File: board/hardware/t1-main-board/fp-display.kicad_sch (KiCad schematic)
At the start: 7 parts, among them U5901 TPS22945DCKR

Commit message: Board: capture blk.maskrom
Power + Vol- at a cold power-on pull eMMC D0 low inside the TPS3808G01
boot window (BOM v1 lines 35, 78, 97, 98; sim/maskrom): SENSE 280k/100k,
CT 390 nF, WINDOW_N with its pad, SN74LVC1G57 and SN74LVC1G58 on
vcca1v8_pmu, BAT54 from PWRON_N, DMG1012T through 1 kΩ to EMMC_D0.
Every block in use now has its sheet; the README states the remaining
single-pin nets.

Co-Authored-By: Claude Opus 5.5 <noreply@anthropic.com>
Claude-Session: https://claude.ai/code/session_01Ei262h3TpgY9vyfNLMi5Mn
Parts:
- removed C5901, C5902: 1 µF, Capacitor_SMD:C_0402_1005Metric, symbol Device:C
- removed R5901: 10 kΩ, Resistor_SMD:R_0402_1005Metric, symbol Device:R
- removed R5902: 100 mΩ, Resistor_SMD:R_0603_1608Metric, symbol Device:R
- removed TP5901: FP_VCI_SW, TestPoint:TestPoint_Pad_D1.0mm, symbol Connector:TestPoint
- removed TP5902: FP_VCI, TestPoint:TestPoint_Pad_D1.0mm, symbol Connector:TestPoint
- removed U5901: TPS22945DCKR, Texas_Instruments:Texas_DCK0005A_SC-70-5_1.25x2mm_P0.65mm, symbol Texas_Instruments:TPS22945DCKR
- added C6001, C6002: 1 µF, Capacitor_SMD:C_0402_1005Metric, symbol Device:C
- added R6001: 10 kΩ, Resistor_SMD:R_0402_1005Metric, symbol Device:R
- added R6002: 100 mΩ, Resistor_SMD:R_0603_1608Metric, symbol Device:R
- added TP6001: FP_VCI_SW, TestPoint:TestPoint_Pad_D1.0mm, symbol Connector:TestPoint
- added TP6002: FP_VCI, TestPoint:TestPoint_Pad_D1.0mm, symbol Connector:TestPoint
- added U6001: TPS22945DCKR, Texas_Instruments:Texas_DCK0005A_SC-70-5_1.25x2mm_P0.65mm, symbol Texas_Instruments:TPS22945DCKR
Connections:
- net FP_IO_EN: now also U6001.4 (ON)
- net FP_VCI: now also R6002.2, TP6002.1
- net FP_VCI_SRC: now also C6001.1, U6001.5 (VIN)
- net FP_VCI_SW: now also C6002.1, R6001.1, R6002.1, TP6001.1, U6001.1 (VOUT)
- net GND: now also C6001.2, C6002.2, R6001.2, U6001.2 (GND)
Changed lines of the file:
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@@
 (title_block (title "Faceplate display supply") (date "2026-10-25") (rev "A") (company "The OpenDAP Project") (comment 1 "blk.fp-display") (comment 2 "FP_VCI current-limited switch after RK809 LDO4; DSI lanes pass to the connector"))
 (symbol (lib_id "Texas_Instruments:TPS22945DCKR") (at 48.26 60.96 0) (unit 1) (body_style 1) (exclude_from_sim no) (in_bom yes) (on_board yes) (dnp no)
-  (property "Reference" "U5901" (at 49.53 45.72 0) (effects (font (size 1.27 1.27)) (justify left)))
+  (property "Reference" "U6001" (at 49.53 45.72 0) (effects (font (size 1.27 1.27)) (justify left)))
   (property "Value" "TPS22945DCKR" (at 49.53 43.18 0) (effects (font (size 1.27 1.27)) (justify left)))
   (property "Footprint" "Texas_Instruments:Texas_DCK0005A_SC-70-5_1.25x2mm_P0.65mm" (at 48.26 60.96 0) (effects (font (size 1.27 1.27))) (hide yes))
@@
   (pin "5")
   (pin "2")
-  (instances (project "t1-main-board" (path "/7746052e-d7f9-59ad-ba73-bd2b74439529/996ec8da-1510-50ce-b9cf-a8f3bb19efac" (reference "U5901") (unit 1))))
+  (instances (project "t1-main-board" (path "/7746052e-d7f9-59ad-ba73-bd2b74439529/996ec8da-1510-50ce-b9cf-a8f3bb19efac" (reference "U6001") (unit 1))))
 )
 (wire (pts (xy 38.1 60.96) (xy 35.56 60.96)) (stroke (width 0) (type default)))
@@
 )
 (symbol (lib_id "Device:C") (at 77.47 55.88 0) (unit 1) (body_style 1) (exclude_from_sim no) (in_bom yes) (on_board yes) (dnp no)
-  (property "Reference" "C5901" (at 80.01 54.61 0) (effects (font (size 1.27 1.27)) (justify left)))
+  (property "Reference" "C6001" (at 80.01 54.61 0) (effects (font (size 1.27 1.27)) (justify left)))
   (property "Value" "1 µF" (at 80.01 57.15 0) (effects (font (size 1.27 1.27)) (justify left)))
   (property "Footprint" "Capacitor_SMD:C_0402_1005Metric" (at 77.47 55.88 0) (effects (font (size 1.27 1.27))) (hide yes))
@@
   (pin "1")
   (pin "2")
-  (instances (project "t1-main-board" (path "/7746052e-d7f9-59ad-ba73-bd2b74439529/996ec8da-1510-50ce-b9cf-a8f3bb19efac" (reference "C5901") (unit 1))))
+  (instances (project "t1-main-board" (path "/7746052e-d7f9-59ad-ba73-bd2b74439529/996ec8da-1510-50ce-b9cf-a8f3bb19efac" (reference "C6001") (unit 1))))
 )
 (wire (pts (xy 77.47 52.07) (xy 77.47 49.53)) (stroke (width 0) (type default)))
@@
 )
 (symbol (lib_id "Device:C") (at 90.17 55.88 0) (unit 1) (body_style 1) (exclude_from_sim no) (in_bom yes) (on_board yes) (dnp no)
-  (property "Reference" "C5902" (at 92.71 54.61 0) (effects (font (size 1.27 1.27)) (justify left)))
+  (property "Reference" "C6002" (at 92.71 54.61 0) (effects (font (size 1.27 1.27)) (justify left)))
   (property "Value" "1 µF" (at 92.71 57.15 0) (effects (font (size 1.27 1.27)) (justify left)))
   (property "Footprint" "Capacitor_SMD:C_0402_1005Metric" (at 90.17 55.88 0) (effects (font (size 1.27 1.27))) (hide yes))
@@
   (pin "1")
   (pin "2")
-  (instances (project "t1-main-board" (path "/7746052e-d7f9-59ad-ba73-bd2b74439529/996ec8da-1510-50ce-b9cf-a8f3bb19efac" (reference "C5902") (unit 1))))
+  (instances (project "t1-main-board" (path "/7746052e-d7f9-59ad-ba73-bd2b74439529/996ec8da-1510-50ce-b9cf-a8f3bb19efac" (reference "C6002") (unit 1))))
 )
 (wire (pts (xy 90.17 52.07) (xy 90.17 49.53)) (stroke (width 0) (type default)))
@@
 )
 (symbol (lib_id "Device:R") (at 102.87 55.88 0) (unit 1) (body_style 1) (exclude_from_sim no) (in_bom yes) (on_board yes) (dnp no)
-  (property "Reference" "R5901" (at 104.14 54.61 0) (effects (font (size 1.27 1.27)) (justify left)))
+  (property "Reference" "R6001" (at 104.14 54.61 0) (effects (font (size 1.27 1.27)) (justify left)))
   (property "Value" "10 kΩ" (at 104.14 57.15 0) (effects (font (size 1.27 1.27)) (justify left)))
   (property "Footprint" "Resistor_SMD:R_0402_1005Metric" (at 102.87 55.88 0) (effects (font (size 1.27 1.27))) (hide yes))
@@
   (pin "1")
   (pin "2")
-  (instances (project "t1-main-board" (path "/7746052e-d7f9-59ad-ba73-bd2b74439529/996ec8da-1510-50ce-b9cf-a8f3bb19efac" (reference "R5901") (unit 1))))
+  (instances (project "t1-main-board" (path "/7746052e-d7f9-59ad-ba73-bd2b74439529/996ec8da-1510-50ce-b9cf-a8f3bb19efac" (reference "R6001") (unit 1))))
 )
 (wire (pts (xy 102.87 52.07) (xy 102.87 49.53)) (stroke (width 0) (type default)))
@@
 (text "FP_VCI: TPS22945 after RK809 LDO4 (BOM v1 line 146)" (exclude_from_sim no) (at 24.13 34.29 0) (effects (font (size 2.54 2.54)) (justify left bottom)))
 (symbol (lib_id "Device:R") (at 181.61 50.8 90) (unit 1) (body_style 1) (exclude_from_sim no) (in_bom yes) (on_board yes) (dnp no)
-  (property "Reference" "R5902" (at 179.07 46.99 90) (effects (font (size 1.27 1.27))))
+  (property "Reference" "R6002" (at 179.07 46.99 90) (effects (font (size 1.27 1.27))))
   (property "Value" "100 mΩ" (at 179.07 53.34 90) (effects (font (size 1.27 1.27))))
   (property "Spec" "0603" (at 179.07 55.88 90) (effects (font (size 1.27 1.27))))
@@
   (pin "1")
   (pin "2")
-  (instances (project "t1-main-board" (path "/7746052e-d7f9-59ad-ba73-bd2b74439529/996ec8da-1510-50ce-b9cf-a8f3bb19efac" (reference "R5902") (unit 1) (variant (name "production") (field (name "Value") (value "0 Ω")) (field (name "MPN") (value "RC0603JR-070RL")) (field (name "Manufacturer") (value "YAGEO"))))))
+  (instances (project "t1-main-board" (path "/7746052e-d7f9-59ad-ba73-bd2b74439529/996ec8da-1510-50ce-b9cf-a8f3bb19efac" (reference "R6002") (unit 1) (variant (name "production") (field (name "Value") (value "0 Ω")) (field (name "MPN") (value "RC0603JR-070RL")) (field (name "Manufacturer") (value "YAGEO"))))))
 )
 (rectangle (start 161.29 38.1) (end 198.12 58.42) (stroke (width 0) (type dash)) (fill (type none)))
@@
 (wire (pts (xy 175.26 50.8) (xy 175.26 48.26)) (stroke (width 0) (type default)))
 (symbol (lib_id "Connector:TestPoint") (at 175.26 48.26 0) (unit 1) (body_style 1) (exclude_from_sim no) (in_bom no) (on_board yes) (dnp no)
-  (property "Reference" "TP5901" (at 173.99 43.18 0) (effects (font (size 1.27 1.27)) (justify right)))
+  (property "Reference" "TP6001" (at 173.99 43.18 0) (effects (font (size 1.27 1.27)) (justify right)))
   (property "Value" "FP_VCI_SW" (at 173.99 45.72 0) (effects (font (size 1.27 1.27)) (justify right)))
   (property "Footprint" "TestPoint:TestPoint_Pad_D1.0mm" (at 175.26 48.26 0) (effects (font (size 1.27 1.27))) (hide yes))
@@
   (property "Block" "blk.fp-display" (at 175.26 48.26 0) (effects (font (size 1.27 1.27))) (hide yes))
   (pin "1")
-  (instances (project "t1-main-board" (path "/7746052e-d7f9-59ad-ba73-bd2b74439529/996ec8da-1510-50ce-b9cf-a8f3bb19efac" (reference "TP5901") (unit 1))))
+  (instances (project "t1-main-board" (path "/7746052e-d7f9-59ad-ba73-bd2b74439529/996ec8da-1510-50ce-b9cf-a8f3bb19efac" (reference "TP6001") (unit 1))))
 )
 (wire (pts (xy 185.42 50.8) (xy 210.82 50.8)) (stroke (width 0) (type default)))
@@
 (wire (pts (xy 187.96 50.8) (xy 187.96 48.26)) (stroke (width 0) (type default)))
 (symbol (lib_id "Connector:TestPoint") (at 187.96 48.26 0) (unit 1) (body_style 1) (exclude_from_sim no) (in_bom no) (on_board yes) (dnp no)
-  (property "Reference" "TP5902" (at 189.23 43.18 0) (effects (font (size 1.27 1.27)) (justify left)))
+  (property "Reference" "TP6002" (at 189.23 43.18 0) (effects (font (size 1.27 1.27)) (justify left)))
   (property "Value" "FP_VCI" (at 189.23 45.72 0) (effects (font (size 1.27 1.27)) (justify left)))
   (property "Footprint" "TestPoint:TestPoint_Pad_D1.0mm" (at 187.96 48.26 0) (effects (font (size 1.27 1.27))) (hide yes))
@@
   (property "Block" "blk.fp-display" (at 187.96 48.26 0) (effects (font (size 1.27 1.27))) (hide yes))
   (pin "1")
-  (instances (project "t1-main-board" (path "/7746052e-d7f9-59ad-ba73-bd2b74439529/996ec8da-1510-50ce-b9cf-a8f3bb19efac" (reference "TP5902") (unit 1))))
+  (instances (project "t1-main-board" (path "/7746052e-d7f9-59ad-ba73-bd2b74439529/996ec8da-1510-50ce-b9cf-a8f3bb19efac" (reference "TP6002") (unit 1))))
 )
 (symbol (lib_id "power:VCC") (at 210.82 50.8 270) (unit 1) (body_style 1) (exclude_from_sim no) (in_bom yes) (on_board yes) (dnp no)

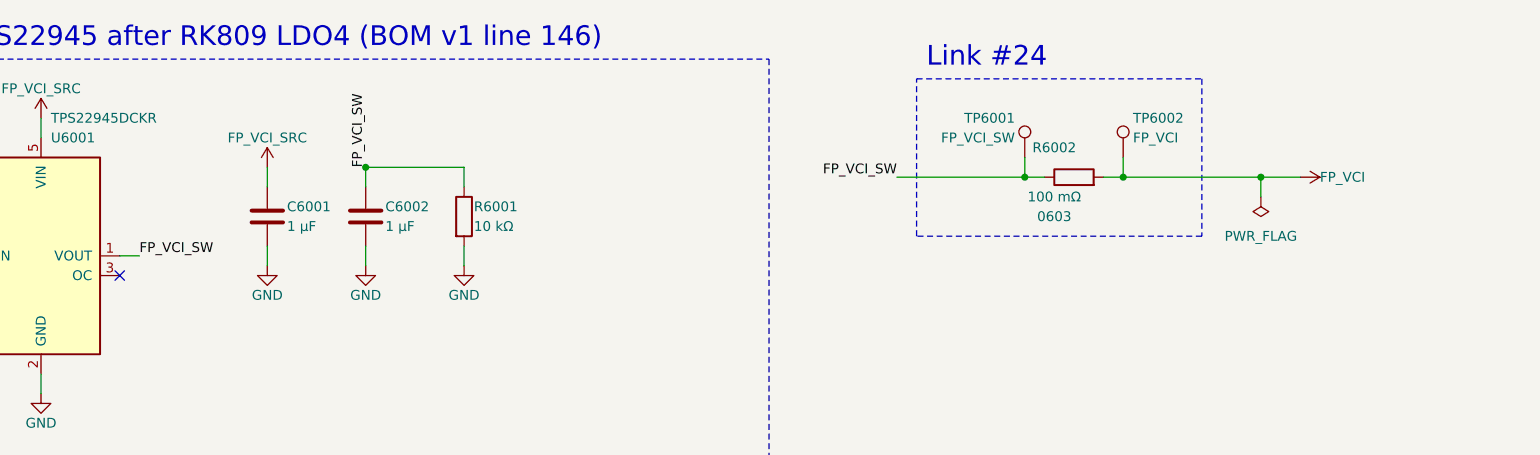
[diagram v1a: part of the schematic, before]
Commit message: Zone net classes and named switch nodes from the generator
Every net but GND now carries the ZONE_<NAME> class of each zone whose
blocks it touches (block zones from pcb/plan.py; the faceplate connector's
sheet also the faceplate zone); a rail used in more than one zone carries
ZONE_SHARED. Nets KiCad names from a pin take their part's sheet zone.
1,080 nets: 911 in one zone, 104 in two, 36 in three, 28 shared rails.

Switch nodes are named *_SW (VSYS_LV_SW, VCC3V3_SYS_SW, VDD_CPU_SW,
RP_VREG_SW); the display switch output is FP_VCI_OUT, so SW_NODE holds
the 18 switch nodes only. Board rebuilt: DRC 0 errors, 607 warnings
(the six PCB-I-09 gone), ERC 0 errors, craft Q1 met, pcb tests pass.
Closes placement v1 open items 2 and 3, floorplan v1 item 6.

Co-Authored-By: Claude Opus 5.5 <noreply@anthropic.com>
Claude-Session: https://claude.ai/code/session_01Ei262h3TpgY9vyfNLMi5Mn
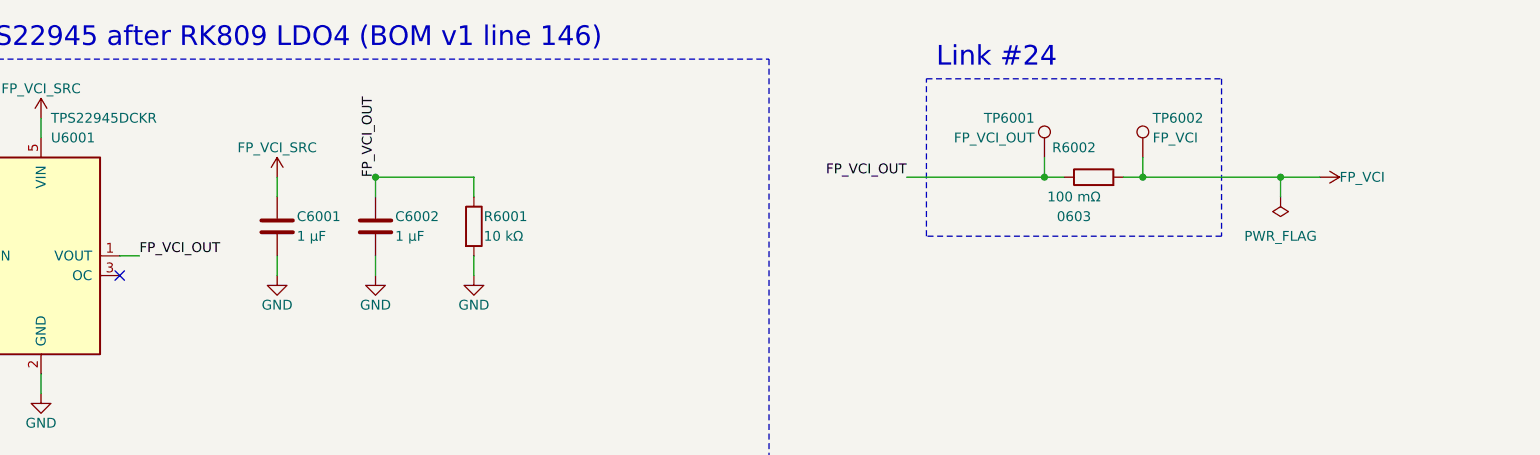
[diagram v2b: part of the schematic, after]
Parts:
- TP6001: value FP_VCI_SW -> FP_VCI_OUT
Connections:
- net FP_VCI_SW renamed FP_VCI_OUT
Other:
- moved on the sheet: C6001, C6002, R6001, R6002, TP6001, TP6002

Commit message: Board on libs v0.2.0: lower-case kebab vendor keys (HL-13)
The libs submodule moves to v0.2.0 (5f24483). Every library nickname in
the generator, the placement tool and the floorplan study follows the
key table (Texas_Instruments -> texas-instruments, OpenDAP_Device ->
opendap-generic, Rockchip and Rockchip_PMIC -> rockchip, ...); the
library tables are written from the files. Schematic and board
regenerated.

Checks: ERC 0 errors (warnings unchanged); DRC 0 errors, 605 warnings,
the same counts by type, schematic parity 0; every placement identical;
craft Q1 met; pcb tests pass; STEP export resolves every libs 3D model
(the 27 parts without a model are KiCad stock lands that have none).

Co-Authored-By: Claude Opus 5.5 <noreply@anthropic.com>
Claude-Session: https://claude.ai/code/session_01Ei262h3TpgY9vyfNLMi5Mn
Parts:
- U6001: footprint Texas_Instruments:Texas_DCK0005A_SC-70-5_1.25x2mm_P0.65mm -> texas-instruments:Texas_DCK0005A_SC-70-5_1.25x2mm_P0.65mm; symbol Texas_Instruments:TPS22945DCKR -> texas-instruments:TPS22945DCKR
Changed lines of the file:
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@@
 (paper "A4")
 (title_block (title "Faceplate display supply") (date "2026-10-25") (rev "A") (company "The OpenDAP Project") (comment 1 "blk.fp-display") (comment 2 "FP_VCI current-limited switch after RK809 LDO4; DSI lanes pass to the connector"))
-(symbol (lib_id "Texas_Instruments:TPS22945DCKR") (at 48.26 60.96 0) (unit 1) (body_style 1) (exclude_from_sim no) (in_bom yes) (on_board yes) (dnp no)
+(symbol (lib_id "texas-instruments:TPS22945DCKR") (at 48.26 60.96 0) (unit 1) (body_style 1) (exclude_from_sim no) (in_bom yes) (on_board yes) (dnp no)
   (property "Reference" "U6001" (at 49.53 45.72 0) (effects (font (size 1.27 1.27)) (justify left)))
   (property "Value" "TPS22945DCKR" (at 49.53 43.18 0) (effects (font (size 1.27 1.27)) (justify left)))
-  (property "Footprint" "Texas_Instruments:Texas_DCK0005A_SC-70-5_1.25x2mm_P0.65mm" (at 48.26 60.96 0) (effects (font (size 1.27 1.27))) (hide yes))
+  (property "Footprint" "texas-instruments:Texas_DCK0005A_SC-70-5_1.25x2mm_P0.65mm" (at 48.26 60.96 0) (effects (font (size 1.27 1.27))) (hide yes))
   (property "Datasheet" "https://www.ti.com/lit/ds/symlink/tps22945.pdf" (at 48.26 60.96 0) (effects (font (size 1.27 1.27))) (hide yes))
   (property "Description" "Current-limited load switch, 1.62-5.5 V, 0.4 Ohm P-channel, 100-200 mA limit, 10 ms blanking, 80 ms auto-restart, active-high ON, open-drain OC flag, SC-70-5 (DCK0005A)" (at 48.26 60.96 0) (effects (font (size 1.27 1.27))) (hide yes))

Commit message: Board in the 62.5 x 95.0 mm body: ADR 0025, outline 59.1 x 91.6, 0201 swaps
ADR 0025 supersedes ADR 0016 for t1 ADR 0006's body: board outline from
the body, 1.2 mm walls and 0.5 mm clearance; height zones and stack
restated unchanged; the speaker on a case shelf (PCB-Z-09); pocket
reliefs at the 4.4 mm jack, the microSD (DM3AT push-push kept) and the
side buttons; the audio 0603 -> 0402 swap gated by t1 V2-A08; reserve
(NFC reader, then TPM) recorded, not applied.

- pcb/geometry.py derives the outline from BODY, WALL and CLEARANCE;
  the pocket, display and fixed parts keep their device-frame positions;
  holes keep their edge distance; the speaker shadow becomes a 1.5 mm
  shelf height area (placement, checks, occupancy).
- build.py reports pocket reliefs and routing room; C904 unfixed (it
  now finds back room, so PCB-Z-04 carries no part).
- Generator: parts.area_swap puts 121 generic 0402 resistors (outside
  audio and VBUS paths, >= 10 ohm) and five 100 nF signal capacitors in
  0201 (BOM v1.16); schematic and board regenerated.
- Result: 1,012/1,012 placed, 98.8 % by the floorplan method (was 111 %),
  factor left 1.68 (was 1.49); DRC 0 errors, ERC 0 errors, 0 check
  findings, pcb tests 20/20, schematic craft Q1 met.
- Specs: PCB constraints v0.17 (M-01, M-02, M-08, Z-02, Z-06 to Z-09,
  R-07), placement v1.1 (section 3, decisions 4 and 13, checks, open
  items with the gated swaps and the reserve), floorplan v1 section 1,
  BOM v1.16.

Co-Authored-By: Claude Opus 5.5 <noreply@anthropic.com>
Claude-Session: https://claude.ai/code/session_01Ei262h3TpgY9vyfNLMi5Mn
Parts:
- R6001: footprint Resistor_SMD:R_0402_1005Metric -> Resistor_SMD:R_0201_0603Metric; MPN RC0402FR-0710KL -> RC0201FR-0710KL
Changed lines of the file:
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@@
   (property "Reference" "R6001" (at 105.41 55.88 0) (effects (font (size 1.27 1.27)) (justify left)))
   (property "Value" "10 kΩ" (at 105.41 58.42 0) (effects (font (size 1.27 1.27)) (justify left)))
-  (property "Footprint" "Resistor_SMD:R_0402_1005Metric" (at 104.14 57.15 0) (effects (font (size 1.27 1.27))) (hide yes))
-  (property "Datasheet" "https://yageogroup.com/en/ProductSearch/PartNumberSearch?part=RC0402FR-0710KL" (at 104.14 57.15 0) (effects (font (size 1.27 1.27))) (hide yes))
-  (property "Description" "Resistor, 10 kΩ, 1 %, 1/16 W, 0402" (at 104.14 57.15 0) (effects (font (size 1.27 1.27))) (hide yes))
+  (property "Footprint" "Resistor_SMD:R_0201_0603Metric" (at 104.14 57.15 0) (effects (font (size 1.27 1.27))) (hide yes))
+  (property "Datasheet" "https://yageogroup.com/en/ProductSearch/PartNumberSearch?part=RC0201FR-0710KL" (at 104.14 57.15 0) (effects (font (size 1.27 1.27))) (hide yes))
+  (property "Description" "Resistor, 10 kΩ, 1 %, 1/20 W, 0201" (at 104.14 57.15 0) (effects (font (size 1.27 1.27))) (hide yes))
   (property "Manufacturer" "YAGEO" (at 104.14 57.15 0) (effects (font (size 1.27 1.27))) (hide yes))
-  (property "MPN" "RC0402FR-0710KL" (at 104.14 57.15 0) (effects (font (size 1.27 1.27))) (hide yes))
+  (property "MPN" "RC0201FR-0710KL" (at 104.14 57.15 0) (effects (font (size 1.27 1.27))) (hide yes))
   (property "Block" "blk.fp-display" (at 104.14 57.15 0) (effects (font (size 1.27 1.27))) (hide yes))
   (pin "1")

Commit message: BOM v1.18 item 2: successors of the discontinued 1 uF 0402
GRM155R61A105KE15D is to be discontinued. 44 positions take
GRM155C71A105KE11D (1 uF 10 V X7S); the eight TPS7A20 positions take
GRM155R61C225KE11D (2.2 uF 16 V X5R) to keep the 0.47 uF effective
minimum with 10 % to spare at up to 3.8 V. Same land; sourcing pass.
Closes BOM §7 item 52; new item 55 lists the other capture parts outside
Murata's product data or near end of life.

Co-Authored-By: Claude Opus 5.5 <noreply@anthropic.com>
Claude-Session: https://claude.ai/code/session_01Ei262h3TpgY9vyfNLMi5Mn
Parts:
- C6001, C6002: MPN GRM155R61A105KE15D -> GRM155C71A105KE11D
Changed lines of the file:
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@@
   (property "Value" "1 µF" (at 81.28 58.42 0) (effects (font (size 1.27 1.27)) (justify left)))
   (property "Footprint" "Capacitor_SMD:C_0402_1005Metric" (at 78.74 57.15 0) (effects (font (size 1.27 1.27))) (hide yes))
-  (property "Datasheet" "https://www.murata.com/en-us/products/productdetail?partno=GRM155R61A105KE15D" (at 78.74 57.15 0) (effects (font (size 1.27 1.27))) (hide yes))
-  (property "Description" "Capacitor, 1 µF, 10 V, X5R, 0402" (at 78.74 57.15 0) (effects (font (size 1.27 1.27))) (hide yes))
+  (property "Datasheet" "https://www.murata.com/en-us/products/productdetail?partno=GRM155C71A105KE11D" (at 78.74 57.15 0) (effects (font (size 1.27 1.27))) (hide yes))
+  (property "Description" "Capacitor, 1 µF, 10 V, X7S, 0402" (at 78.74 57.15 0) (effects (font (size 1.27 1.27))) (hide yes))
   (property "Manufacturer" "Murata" (at 78.74 57.15 0) (effects (font (size 1.27 1.27))) (hide yes))
-  (property "MPN" "GRM155R61A105KE15D" (at 78.74 57.15 0) (effects (font (size 1.27 1.27))) (hide yes))
+  (property "MPN" "GRM155C71A105KE11D" (at 78.74 57.15 0) (effects (font (size 1.27 1.27))) (hide yes))
   (property "Block" "blk.fp-display" (at 78.74 57.15 0) (effects (font (size 1.27 1.27))) (hide yes))
   (pin "1")
@@
   (property "Value" "1 µF" (at 93.98 58.42 0) (effects (font (size 1.27 1.27)) (justify left)))
   (property "Footprint" "Capacitor_SMD:C_0402_1005Metric" (at 91.44 57.15 0) (effects (font (size 1.27 1.27))) (hide yes))
-  (property "Datasheet" "https://www.murata.com/en-us/products/productdetail?partno=GRM155R61A105KE15D" (at 91.44 57.15 0) (effects (font (size 1.27 1.27))) (hide yes))
-  (property "Description" "Capacitor, 1 µF, 10 V, X5R, 0402" (at 91.44 57.15 0) (effects (font (size 1.27 1.27))) (hide yes))
+  (property "Datasheet" "https://www.murata.com/en-us/products/productdetail?partno=GRM155C71A105KE11D" (at 91.44 57.15 0) (effects (font (size 1.27 1.27))) (hide yes))
+  (property "Description" "Capacitor, 1 µF, 10 V, X7S, 0402" (at 91.44 57.15 0) (effects (font (size 1.27 1.27))) (hide yes))
   (property "Manufacturer" "Murata" (at 91.44 57.15 0) (effects (font (size 1.27 1.27))) (hide yes))
-  (property "MPN" "GRM155R61A105KE15D" (at 91.44 57.15 0) (effects (font (size 1.27 1.27))) (hide yes))
+  (property "MPN" "GRM155C71A105KE11D" (at 91.44 57.15 0) (effects (font (size 1.27 1.27))) (hide yes))
   (property "Block" "blk.fp-display" (at 91.44 57.15 0) (effects (font (size 1.27 1.27))) (hide yes))
   (pin "1")
